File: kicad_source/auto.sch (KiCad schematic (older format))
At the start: 11 parts, among them U14 NE555, U15 74xx175, U16 74xx00, U17 74xx175, U18 74xx08, U19 74xx32

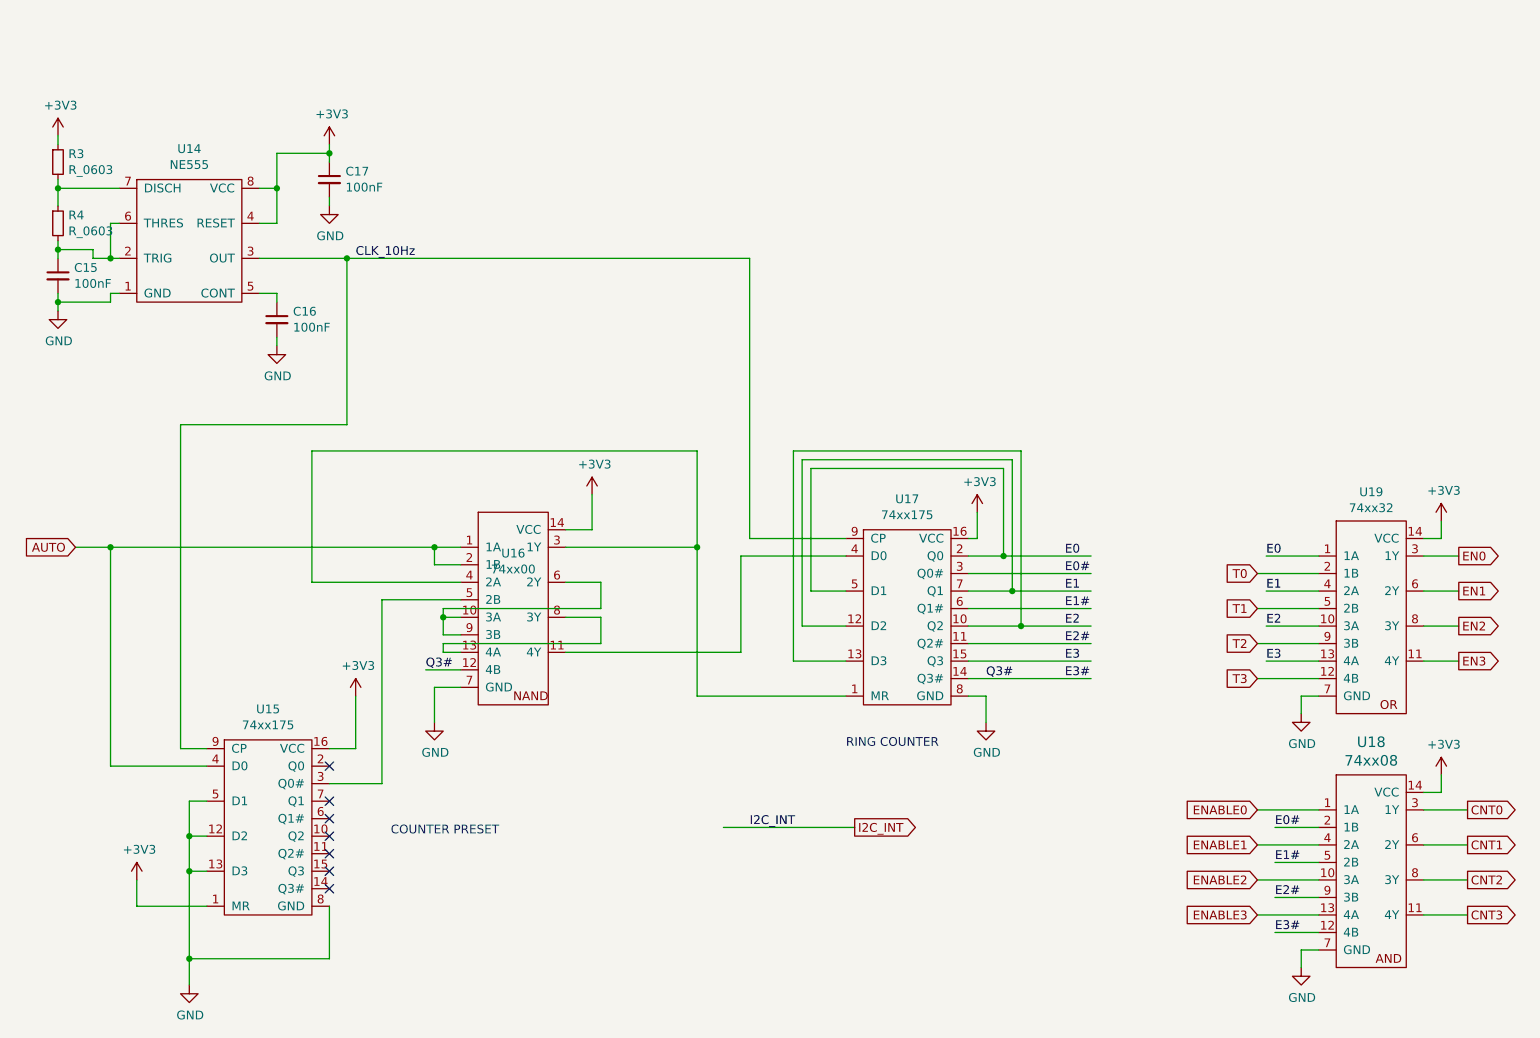
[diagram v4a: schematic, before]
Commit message: schematic changed
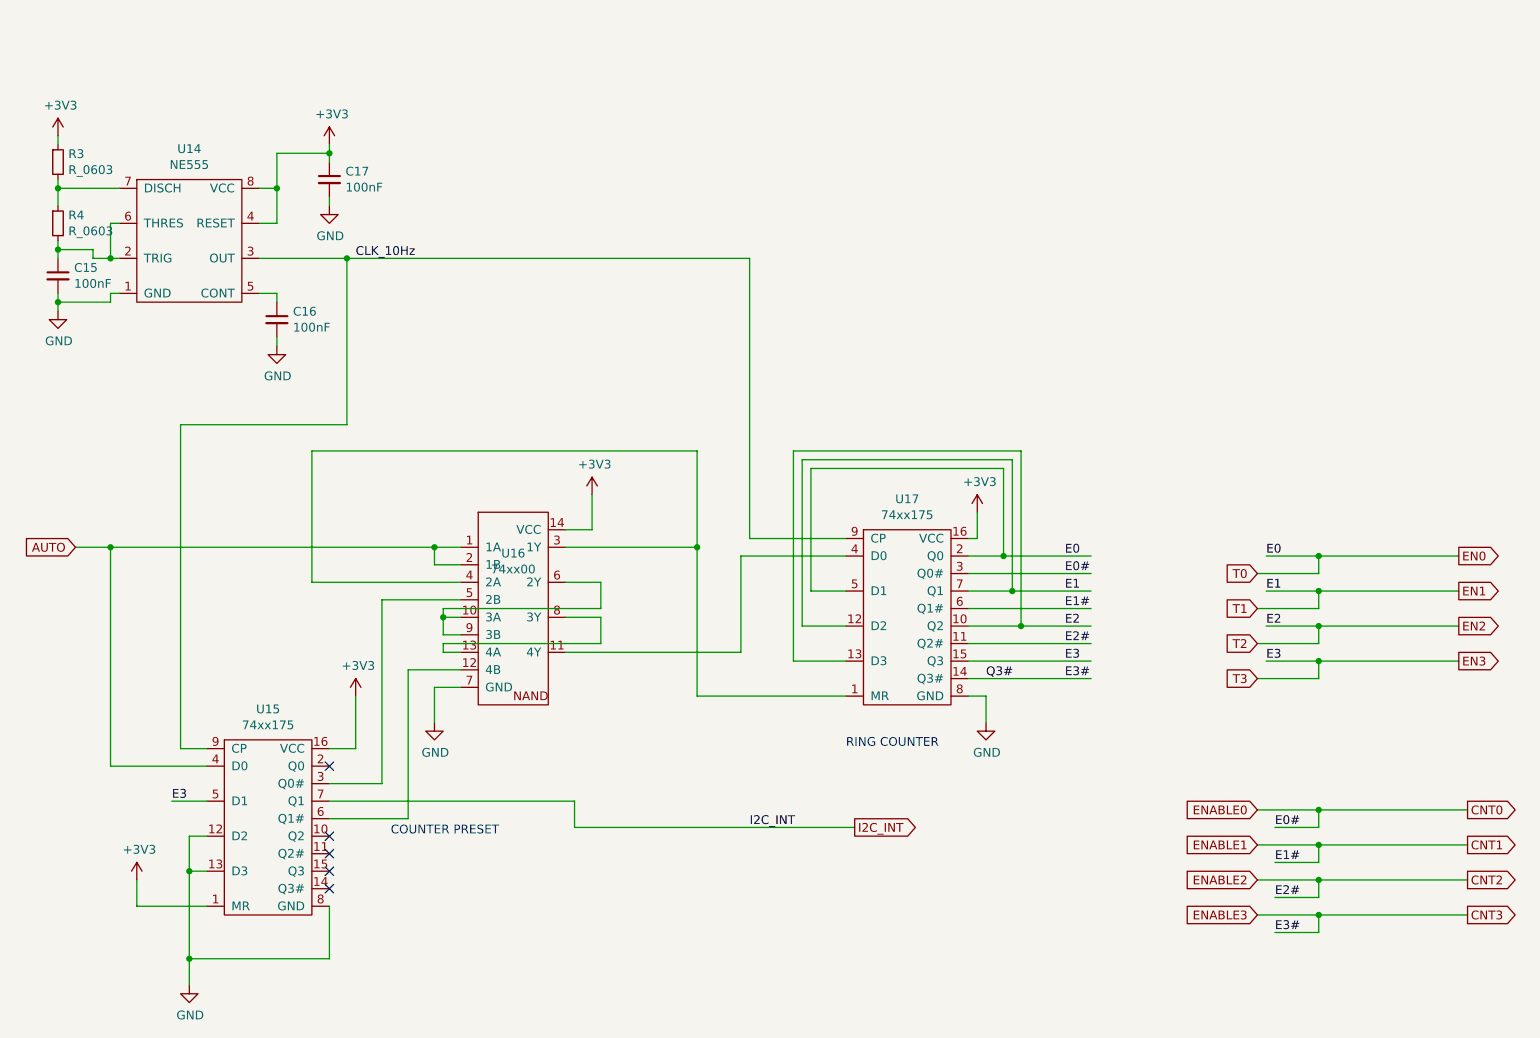
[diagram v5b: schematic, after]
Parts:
- removed U18: 74xx08, SOIC:SOIC-14_3.9x8.7mm_Pitch1.27mm, symbol IC_logic:74xx08
- removed U19: 74xx32, SOIC:SOIC-14_3.9x8.7mm_Pitch1.27mm, symbol IC_logic:74xx32
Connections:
- wire segments 146 -> 149
- no-connect marks 7 -> 5
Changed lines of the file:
@@
 	6100 3350 6100 3900
 Connection ~ 6100 3900
-Wire Wire Line
-	4550 4600 4750 4600
 Text Label 7750 4650 0    50   ~ 0
 Q3#
-Text Label 4550 4600 0    50   ~ 0
-Q3#
 Wire Wire Line
 	5350 4100 5550 4100
@@
 Wire Wire Line
 	4650 4450 5550 4450
-NoConn ~ 4000 5350
 NoConn ~ 4000 5150
-NoConn ~ 4000 5450
 NoConn ~ 4000 5550
 NoConn ~ 4000 5650
@@
 	2900 5950 2900 5800
 Wire Wire Line
-	3300 5350 3200 5350
-Wire Wire Line
-	3200 5350 3200 5550
-Wire Wire Line
 	3300 5550 3200 5550
-Connection ~ 3200 5550
 Wire Wire Line
 	3200 5550 3200 5750
@@
 Text Label 8200 4650 0    50   ~ 0
 E3#
-$Comp
-L IC_logic:74xx32 U19
-U 1 1 5EF4E33D
-P 9900 4850
-F 0 "U19" H 9950 6115 50  0000 C CNN
-F 1 "74xx32" H 9950 6024 50  0000 C CNN
-F 2 "SOIC:SOIC-14_3.9x8.7mm_Pitch1.27mm" H 9900 4850 50  0001 C CNN
-F 3 "" H 9900 4850 50  0001 C CNN
-	1    9900 4850
-	1    0    0    -1
-$EndComp
-Wire Wire Line
-	10250 3950 10450 3950
-Wire Wire Line
-	10250 4150 10450 4150
-Wire Wire Line
-	10250 4350 10450 4350
-Wire Wire Line
-	10250 4550 10450 4550
-Wire Wire Line
-	9650 3950 9350 3950
 Wire Wire Line
 	9650 4050 9300 4050
 Wire Wire Line
-	9650 4150 9350 4150
-Wire Wire Line
 	9650 4250 9300 4250
 Wire Wire Line
-	9650 4350 9350 4350
-Wire Wire Line
 	9650 4450 9300 4450
-Wire Wire Line
-	9650 4550 9350 4550
 Wire Wire Line
 	9650 4650 9300 4650
@@
 Text Label 9350 4550 0    50   ~ 0
 E3
-$Comp
-L IC_logic:74xx08 U18
-U 1 1 5EF82717
-P 9750 5700
-F 0 "U18" H 9950 6387 60  0000 C CNN
-F 1 "74xx08" H 9950 6281 60  0000 C CNN
-F 2 "SOIC:SOIC-14_3.9x8.7mm_Pitch1.27mm" H 10050 5550 60  0001 C CNN
-F 3 "" H 9750 5700 60  0000 C CNN
-	1    9750 5700
-	1    0    0    -1
-$EndComp
-Wire Wire Line
-	10250 5400 10500 5400
-Wire Wire Line
-	10250 5600 10500 5600
-Wire Wire Line
-	10250 5800 10500 5800
-Wire Wire Line
-	10250 6000 10500 6000
 Text GLabel 10500 5400 2    50   Output ~ 0
 CNT0
@@
 Text GLabel 10500 6000 2    50   Output ~ 0
 CNT3
-Wire Wire Line
-	9650 5400 9300 5400
-Wire Wire Line
-	9650 5600 9300 5600
-Wire Wire Line
-	9650 5800 9300 5800
-Wire Wire Line
-	9650 6000 9300 6000
 Text GLabel 9300 5400 0    50   Input ~ 0
 ENABLE0
@@
 Text Label 9400 6100 0    50   ~ 0
 E3#
-Wire Wire Line
-	10250 3850 10350 3850
-Wire Wire Line
-	10350 3850 10350 3750
-Wire Wire Line
-	9650 4750 9550 4750
-Wire Wire Line
-	9550 4750 9550 4850
-Wire Wire Line
-	10250 5300 10350 5300
-Wire Wire Line
-	10350 5300 10350 5200
-Wire Wire Line
-	9650 6200 9550 6200
-Wire Wire Line
-	9550 6200 9550 6300
-$Comp
-L power-supply:+3V3 #PWR062
-U 1 1 5EFF69D6
-P 10350 3750
-F 0 "#PWR062" H 10350 3600 50  0001 C CNN
-F 1 "+3V3" H 10365 3923 50  0000 C CNN
-F 2 "" H 10350 3750 50  0000 C CNN
-F 3 "" H 10350 3750 50  0000 C CNN
-	1    10350 3750
-	1    0    0    -1
-$EndComp
-$Comp
-L power-supply:GND #PWR060
-U 1 1 5EFF6F21
-P 9550 4850
-F 0 "#PWR060" H 9550 4600 50  0001 C CNN
-F 1 "GND" H 9555 4677 50  0000 C CNN
-F 2 "" H 9550 4850 50  0000 C CNN
-F 3 "" H 9550 4850 50  0000 C CNN
-	1    9550 4850
-	1    0    0    -1
-$EndComp
-$Comp
-L power-supply:+3V3 #PWR063
-U 1 1 5EFF73E0
-P 10350 5200
-F 0 "#PWR063" H 10350 5050 50  0001 C CNN
-F 1 "+3V3" H 10365 5373 50  0000 C CNN
-F 2 "" H 10350 5200 50  0000 C CNN
-F 3 "" H 10350 5200 50  0000 C CNN
-	1    10350 5200
-	1    0    0    -1
-$EndComp
-$Comp
-L power-supply:GND #PWR061
-U 1 1 5EFF7A2D
-P 9550 6300
-F 0 "#PWR061" H 9550 6050 50  0001 C CNN
-F 1 "GND" H 9555 6127 50  0000 C CNN
-F 2 "" H 9550 6300 50  0000 C CNN
-F 3 "" H 9550 6300 50  0000 C CNN
-	1    9550 6300
-	1    0    0    -1
-$EndComp
 Text GLabel 7000 5500 2    50   Output ~ 0
 I2C_INT
-Wire Wire Line
-	6250 5500 7000 5500
 Text Label 6400 5500 0    50   ~ 0
 I2C_INT
+Wire Wire Line
+	3300 5350 3100 5350
+Wire Wire Line
+	4000 5450 4450 5450
+Wire Wire Line
+	4450 5450 4450 4600
+Wire Wire Line
+	4450 4600 4750 4600
+Wire Wire Line
+	4000 5350 5400 5350
+Wire Wire Line
+	5400 5350 5400 5500
+Wire Wire Line
+	5400 5500 7000 5500
+Text Label 3100 5350 0    50   ~ 0
+E3
+Wire Wire Line
+	9350 3950 9650 3950
+Wire Wire Line
+	9650 4050 9650 3950
+Connection ~ 9650 3950
+Wire Wire Line
+	9650 3950 10450 3950
+Wire Wire Line
+	9350 4150 9650 4150
+Wire Wire Line
+	9650 4250 9650 4150
+Connection ~ 9650 4150
+Wire Wire Line
+	9650 4150 10450 4150
+Wire Wire Line
+	9350 4350 9650 4350
+Wire Wire Line
+	9650 4450 9650 4350
+Connection ~ 9650 4350
+Wire Wire Line
+	9650 4350 10450 4350
+Wire Wire Line
+	9350 4550 9650 4550
+Wire Wire Line
+	9650 4550 9650 4650
+Connection ~ 9650 4550
+Wire Wire Line
+	9650 4550 10450 4550
+Wire Wire Line
+	9300 5400 9650 5400
+Wire Wire Line
+	9650 5500 9650 5400
+Connection ~ 9650 5400
+Wire Wire Line
+	9650 5400 10500 5400
+Wire Wire Line
+	9300 5600 9650 5600
+Wire Wire Line
+	9650 5700 9650 5600
+Connection ~ 9650 5600
+Wire Wire Line
+	9650 5600 10500 5600
+Wire Wire Line
+	9300 5800 9650 5800
+Wire Wire Line
+	9650 5900 9650 5800
+Connection ~ 9650 5800
+Wire Wire Line
+	9650 5800 10500 5800
+Wire Wire Line
+	9300 6000 9650 6000
+Wire Wire Line
+	9650 6000 9650 6100
+Connection ~ 9650 6000
+Wire Wire Line
+	9650 6000 10500 6000
 $EndSCHEMATC

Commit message: finished pcb layout
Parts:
- added C18, C19, C20, C21, C22: C_0603, capacitors:C_0603, symbol devices:C_0603
- added U18: 74xx32, SOIC:SOIC-14_3.9x8.7mm_Pitch1.27mm, symbol IC_logic:74xx32
- added U3: 74xx08, SOIC:SOIC-14_3.9x8.7mm_Pitch1.27mm, symbol IC_logic:74xx08
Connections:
- wire segments 149 -> 159

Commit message: reacted to review
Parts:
- added D3, D4, D5, D6: Led_Small, LEDs:LED_0603, symbol devices:Led_Small
- added R10, R11, R12, R9: 220, resistors:R_0603, symbol devices:R_0603
- C15: value 100nF -> 1uF
- C16: value 100nF -> 10nF
- C18, C19, C20, C21, C22: value C_0603 -> 100nF
- R3: value R_0603 -> 120k
- R4: value R_0603 -> 12k
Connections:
- wire segments 159 -> 175
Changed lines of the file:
@@
 AR Path="/5EDDA6D0/5EDEF6E1" Ref="C15"  Part="1"
 F 0 "C15" H 2542 2396 50  0000 L CNN
-F 1 "100nF" H 2542 2305 50  0000 L CNN
+F 1 "1uF" H 2542 2305 50  0000 L CNN
 F 2 "capacitors:C_0603" H 2450 2200 50  0001 C CNN
 F 3 "" H 2450 2350 50  0000 C CNN
@@
 AR Path="/5EDDA6D0/5EDEF6E7" Ref="R4"  Part="1"
 F 0 "R4" H 2509 2096 50  0000 L CNN
-F 1 "R_0603" H 2509 2005 50  0000 L CNN
+F 1 "12k" H 2509 2005 50  0000 L CNN
 F 2 "resistors:R_0603" H 2450 1900 50  0001 C CNN
 F 3 "" H 2450 2050 50  0000 C CNN
@@
 AR Path="/5EDDA6D0/5EDEF6ED" Ref="R3"  Part="1"
 F 0 "R3" H 2509 1746 50  0000 L CNN
-F 1 "R_0603" H 2509 1655 50  0000 L CNN
+F 1 "120k" H 2509 1655 50  0000 L CNN
 F 2 "resistors:R_0603" H 2450 1550 50  0001 C CNN
 F 3 "" H 2450 1700 50  0000 C CNN
@@
 AR Path="/5EDDA6D0/5EDEF705" Ref="C16"  Part="1"
 F 0 "C16" H 3792 2646 50  0000 L CNN
-F 1 "100nF" H 3792 2555 50  0000 L CNN
+F 1 "10nF" H 3792 2555 50  0000 L CNN
 F 2 "capacitors:C_0603" H 3700 2450 50  0001 C CNN
 F 3 "" H 3700 2600 50  0000 C CNN
@@
 AR Path="/5EDDA6D0/5EF21697" Ref="C18"  Part="1"
 F 0 "C18" H 2392 5496 50  0000 L CNN
-F 1 "C_0603" H 2392 5405 50  0000 L CNN
+F 1 "100nF" H 2392 5405 50  0000 L CNN
 F 2 "capacitors:C_0603" H 2300 5300 50  0001 C CNN
 F 3 "" H 2300 5450 50  0000 C CNN
@@
 AR Path="/5EDDA6D0/5EF2E43A" Ref="C19"  Part="1"
 F 0 "C19" H 5642 5046 50  0000 L CNN
-F 1 "C_0603" H 5642 4955 50  0000 L CNN
+F 1 "100nF" H 5642 4955 50  0000 L CNN
 F 2 "capacitors:C_0603" H 5550 4850 50  0001 C CNN
 F 3 "" H 5550 5000 50  0000 C CNN
@@
 AR Path="/5EDDA6D0/5EF34F2B" Ref="C20"  Part="1"
 F 0 "C20" H 8392 3196 50  0000 L CNN
-F 1 "C_0603" H 8392 3105 50  0000 L CNN
+F 1 "100nF" H 8392 3105 50  0000 L CNN
 F 2 "capacitors:C_0603" H 8300 3000 50  0001 C CNN
 F 3 "" H 8300 3150 50  0000 C CNN
@@
 AR Path="/5EDDA6D0/5EE68A84" Ref="C22"  Part="1"
 F 0 "C22" H 8942 4846 50  0000 L CNN
-F 1 "C_0603" H 8942 4755 50  0000 L CNN
+F 1 "100nF" H 8942 4755 50  0000 L CNN
 F 2 "capacitors:C_0603" H 8850 4650 50  0001 C CNN
 F 3 "" H 8850 4800 50  0000 C CNN
@@
 AR Path="/5EDDA6D0/5EE6EA2D" Ref="C21"  Part="1"
 F 0 "C21" H 8742 6196 50  0000 L CNN
-F 1 "C_0603" H 8742 6105 50  0000 L CNN
+F 1 "100nF" H 8742 6105 50  0000 L CNN
 F 2 "capacitors:C_0603" H 8650 6000 50  0001 C CNN
 F 3 "" H 8650 6150 50  0000 C CNN
@@
 Wire Wire Line
 	10250 6000 10500 6000
+$Comp
+L devices:R_0603 R?
+U 1 1 5EF55645
+P 9700 1200
+AR Path="/5EF55645" Ref="R?"  Part="1"
+AR Path="/5EDDA6D0/5EF55645" Ref="R9"  Part="1"
+F 0 "R9" H 9759 1246 50  0000 L CNN
+F 1 "220" H 9759 1155 50  0000 L CNN
+F 2 "resistors:R_0603" H 9700 1050 50  0001 C CNN
+F 3 "" H 9700 1200 50  0000 C CNN
+	1    9700 1200
+	0    -1   -1   0
+$EndComp
+$Comp
+L devices:Led_Small D?
+U 1 1 5EF5564B
+P 9950 1200
+AR Path="/5EF5564B" Ref="D?"  Part="1"
+AR Path="/5EDDA6D0/5EF5564B" Ref="D3"  Part="1"
+F 0 "D3" H 9950 905 50  0000 C CNN
+F 1 "Led_Small" H 9950 996 50  0000 C CNN
+F 2 "LEDs:LED_0603" H 9950 1087 50  0000 C CNN
+F 3 "" V 9950 1200 50  0000 C CNN
+	1    9950 1200
+	-1   0    0    1
+$EndComp
+Wire Wire Line
+	9850 1200 9800 1200
+$Comp
+L power-supply:GND #PWR?
+U 1 1 5EF55653
+P 10150 1250
+AR Path="/5EF55653" Ref="#PWR?"  Part="1"
+AR Path="/5EDDA6D0/5EF55653" Ref="#PWR0128"  Part="1"
+F 0 "#PWR0128" H 10150 1000 50  0001 C CNN
+F 1 "GND" H 10155 1077 50  0000 C CNN
+F 2 "" H 10150 1250 50  0000 C CNN
+F 3 "" H 10150 1250 50  0000 C CNN
+	1    10150 1250
+	1    0    0    -1
+$EndComp
+Wire Wire Line
+	10150 1200 10150 1250
+Wire Wire Line
+	10050 1200 10150 1200
+$Comp
+L devices:R_0603 R?
+U 1 1 5EF6B354
+P 9700 1750
+AR Path="/5EF6B354" Ref="R?"  Part="1"
+AR Path="/5EDDA6D0/5EF6B354" Ref="R10"  Part="1"
+F 0 "R10" H 9759 1796 50  0000 L CNN
+F 1 "220" H 9759 1705 50  0000 L CNN
+F 2 "resistors:R_0603" H 9700 1600 50  0001 C CNN
+F 3 "" H 9700 1750 50  0000 C CNN
+	1    9700 1750
+	0    -1   -1   0
+$EndComp
+$Comp
+L devices:Led_Small D?
+U 1 1 5EF6B35A
+P 9950 1750
+AR Path="/5EF6B35A" Ref="D?"  Part="1"
+AR Path="/5EDDA6D0/5EF6B35A" Ref="D4"  Part="1"
+F 0 "D4" H 9950 1455 50  0000 C CNN
+F 1 "Led_Small" H 9950 1546 50  0000 C CNN
+F 2 "LEDs:LED_0603" H 9950 1637 50  0000 C CNN
+F 3 "" V 9950 1750 50  0000 C CNN
+	1    9950 1750
+	-1   0    0    1
+$EndComp
+Wire Wire Line
+	9850 1750 9800 1750
+$Comp
+L power-supply:GND #PWR?
+U 1 1 5EF6B361
+P 10150 1800
+AR Path="/5EF6B361" Ref="#PWR?"  Part="1"
+AR Path="/5EDDA6D0/5EF6B361" Ref="#PWR0129"  Part="1"
+F 0 "#PWR0129" H 10150 1550 50  0001 C CNN
+F 1 "GND" H 10155 1627 50  0000 C CNN
+F 2 "" H 10150 1800 50  0000 C CNN
+F 3 "" H 10150 1800 50  0000 C CNN
+	1    10150 1800
+	1    0    0    -1
+$EndComp
+Wire Wire Line
+	10150 1750 10150 1800
+Wire Wire Line
+	10050 1750 10150 1750
+$Comp
+L devices:R_0603 R?
+U 1 1 5EF72572
+P 9700 2250
+AR Path="/5EF72572" Ref="R?"  Part="1"
+AR Path="/5EDDA6D0/5EF72572" Ref="R11"  Part="1"
+F 0 "R11" H 9759 2296 50  0000 L CNN
+F 1 "220" H 9759 2205 50  0000 L CNN
+F 2 "resistors:R_0603" H 9700 2100 50  0001 C CNN
+F 3 "" H 9700 2250 50  0000 C CNN
+	1    9700 2250
+	0    -1   -1   0
+$EndComp
+$Comp
+L devices:Led_Small D?
+U 1 1 5EF72578
+P 9950 2250
+AR Path="/5EF72578" Ref="D?"  Part="1"
+AR Path="/5EDDA6D0/5EF72578" Ref="D5"  Part="1"
+F 0 "D5" H 9950 1955 50  0000 C CNN
+F 1 "Led_Small" H 9950 2046 50  0000 C CNN
+F 2 "LEDs:LED_0603" H 9950 2137 50  0000 C CNN
+F 3 "" V 9950 2250 50  0000 C CNN
+	1    9950 2250
+	-1   0    0    1
+$EndComp
+Wire Wire Line
+	9850 2250 9800 2250
+$Comp
+L power-supply:GND #PWR?
+U 1 1 5EF7257F
+P 10150 2300
+AR Path="/5EF7257F" Ref="#PWR?"  Part="1"
+AR Path="/5EDDA6D0/5EF7257F" Ref="#PWR0130"  Part="1"
+F 0 "#PWR0130" H 10150 2050 50  0001 C CNN
+F 1 "GND" H 10155 2127 50  0000 C CNN
+F 2 "" H 10150 2300 50  0000 C CNN
+F 3 "" H 10150 2300 50  0000 C CNN
+	1    10150 2300
+	1    0    0    -1
+$EndComp
+Wire Wire Line
+	10150 2250 10150 2300
+Wire Wire Line
+	10050 2250 10150 2250
+$Comp
+L devices:R_0603 R?
+U 1 1 5EF795B4
+P 9700 2750
+AR Path="/5EF795B4" Ref="R?"  Part="1"
+AR Path="/5EDDA6D0/5EF795B4" Ref="R12"  Part="1"
+F 0 "R12" H 9759 2796 50  0000 L CNN
+F 1 "220" H 9759 2705 50  0000 L CNN
+F 2 "resistors:R_0603" H 9700 2600 50  0001 C CNN
+F 3 "" H 9700 2750 50  0000 C CNN
+	1    9700 2750
+	0    -1   -1   0
+$EndComp
+$Comp
+L devices:Led_Small D?
+U 1 1 5EF795BA
+P 9950 2750
+AR Path="/5EF795BA" Ref="D?"  Part="1"
+AR Path="/5EDDA6D0/5EF795BA" Ref="D6"  Part="1"
+F 0 "D6" H 9950 2455 50  0000 C CNN
+F 1 "Led_Small" H 9950 2546 50  0000 C CNN
+F 2 "LEDs:LED_0603" H 9950 2637 50  0000 C CNN
+F 3 "" V 9950 2750 50  0000 C CNN
+	1    9950 2750
+	-1   0    0    1
+$EndComp
+Wire Wire Line
+	9850 2750 9800 2750
+$Comp
+L power-supply:GND #PWR?
+U 1 1 5EF795C1
+P 10150 2800
+AR Path="/5EF795C1" Ref="#PWR?"  Part="1"
+AR Path="/5EDDA6D0/5EF795C1" Ref="#PWR0131"  Part="1"
+F 0 "#PWR0131" H 10150 2550 50  0001 C CNN
+F 1 "GND" H 10155 2627 50  0000 C CNN
+F 2 "" H 10150 2800 50  0000 C CNN
+F 3 "" H 10150 2800 50  0000 C CNN
+	1    10150 2800
+	1    0    0    -1
+$EndComp
+Wire Wire Line
+	10150 2750 10150 2800
+Wire Wire Line
+	10050 2750 10150 2750
+Wire Wire Line
+	9600 2750 9450 2750
+Wire Wire Line
+	9600 2250 9450 2250
+Wire Wire Line
+	9600 1750 9450 1750
+Wire Wire Line
+	9600 1200 9450 1200
+Text GLabel 9450 1200 0    50   Input ~ 0
+CNT0
+Text GLabel 9450 1750 0    50   Input ~ 0
+CNT1
+Text GLabel 9450 2250 0    50   Input ~ 0
+CNT2
+Text GLabel 9450 2750 0    50   Input ~ 0
+CNT3
 $EndSCHEMATC
